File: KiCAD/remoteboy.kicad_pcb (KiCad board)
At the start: 2 copper layers, 47.2 x 129.2 mm, 36 parts, among them Q1 MMBT2222A, SW1 SW_Push, SW10 SW_Push, SW2 SW_Push, SW3 SW_Push, SW4 SW_Push, SW5 SW_Push, SW6 SW_Push, SW7 SW_Push, SW8 SW_Push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

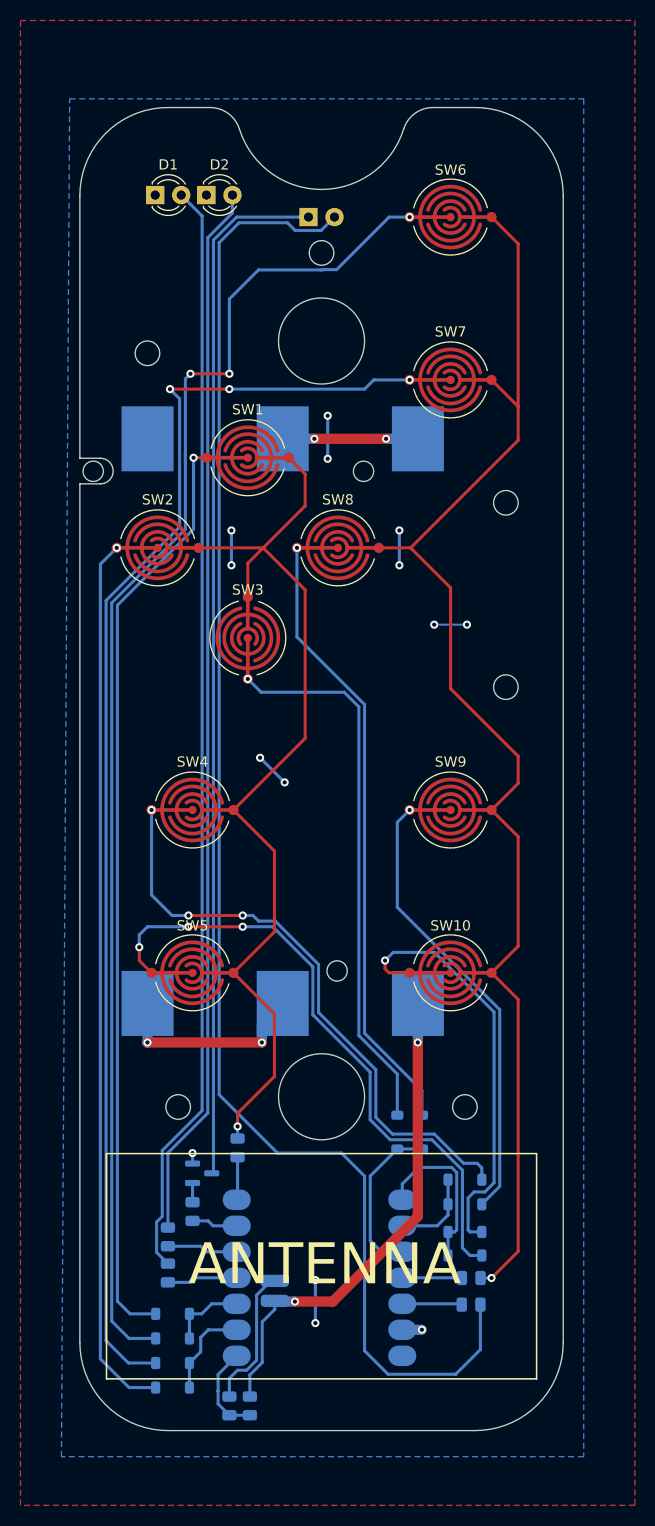
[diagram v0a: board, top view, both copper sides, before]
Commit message: Fix schematic and pcb
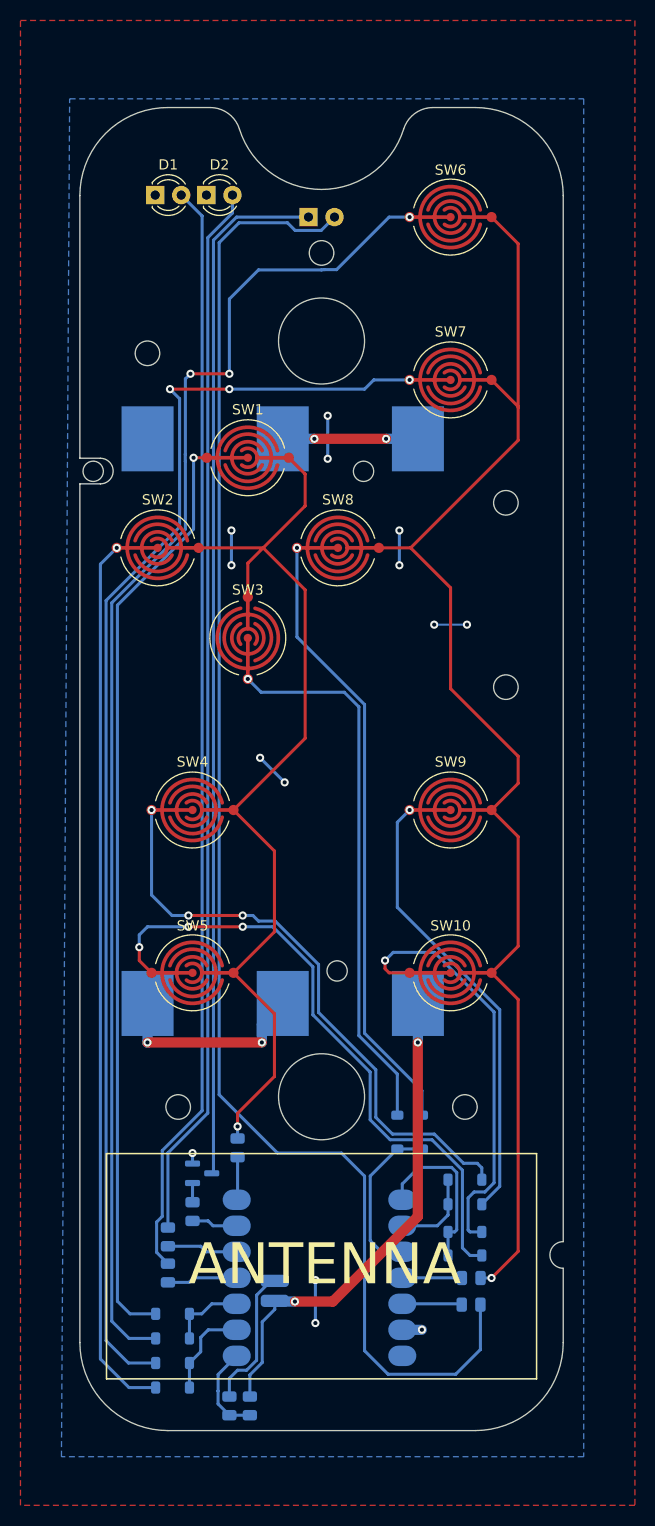
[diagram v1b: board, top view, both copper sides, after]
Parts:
- turned D10 to 0 degrees
- turned D11 to -90 degrees
- turned D12 to 180 degrees
- turned D13 to 180 degrees
- turned D4 to 0 degrees
- turned D5 to 0 degrees
- turned D6 to -90 degrees
- turned D7 to 180 degrees
- turned D8 to 180 degrees
- turned D9 to 0 degrees
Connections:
- D10 pad 1: /ROW2 -> Net-(D10-K)
- D10 pad 2: Net-(D10-A) -> /ROW2
- D11 pad 1: /ROW3 -> Net-(D11-K)
- D11 pad 2: Net-(D11-A) -> /ROW3
- D12 pad 1: /ROW4 -> Net-(D12-K)
- D12 pad 2: Net-(D12-A) -> /ROW4
- D13 pad 1: /ROW5 -> Net-(D13-K)
- D13 pad 2: Net-(D13-A) -> /ROW5
- D4 pad 1: /ROW1 -> Net-(D4-K)
- D4 pad 2: Net-(D4-A) -> /ROW1
- D5 pad 1: /ROW2 -> Net-(D5-K)
- D5 pad 2: Net-(D5-A) -> /ROW2
- D6 pad 1: /ROW3 -> Net-(D6-K)
- D6 pad 2: Net-(D6-A) -> /ROW3
- D7 pad 1: /ROW4 -> Net-(D7-K)
- D7 pad 2: Net-(D7-A) -> /ROW4
- D8 pad 1: /ROW5 -> Net-(D8-K)
- D8 pad 2: Net-(D8-A) -> /ROW5
- D9 pad 1: /ROW1 -> Net-(D9-K)
- D9 pad 2: Net-(D9-A) -> /ROW1
- SW1 pad 1: Net-(D4-A) -> Net-(D4-K)
- SW10 pad 1: Net-(D13-A) -> Net-(D13-K)
- SW2 pad 1: Net-(D5-A) -> Net-(D5-K)
- SW3 pad 1: Net-(D6-A) -> Net-(D6-K)
- SW4 pad 1: Net-(D7-A) -> Net-(D7-K)
- SW5 pad 1: Net-(D8-A) -> Net-(D8-K)
- SW6 pad 1: Net-(D9-A) -> Net-(D9-K)
- SW7 pad 1: Net-(D10-A) -> Net-(D10-K)
- SW8 pad 1: Net-(D11-A) -> Net-(D11-K)
- SW9 pad 1: Net-(D12-A) -> Net-(D12-K)
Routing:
- net Net-(D9-K): track 0.00 -> 132.7 mm, vias 0 -> 3
- net Net-(D9-A): track 132.7 -> 0.00 mm, vias 3 -> 0
- net Net-(D10-K): track 0.00 -> 126.0 mm, vias 0 -> 3
- net Net-(D10-A): track 126.0 -> 0.00 mm, vias 3 -> 0
- net Net-(D4-K): track 0.00 -> 91.0 mm, vias 0 -> 1
- net Net-(D4-A): track 91.0 -> 0.00 mm, vias 1 -> 0
- net Net-(D5-K): track 0.00 -> 86.4 mm, vias 0 -> 1
- net Net-(D5-A): track 86.4 -> 0.00 mm, vias 1 -> 0
- net Net-(D8-K): track 0.00 -> 61.2 mm, vias 0 -> 3
- net Net-(D8-A): track 61.2 -> 0.00 mm, vias 3 -> 0
- net Net-(D11-K): track 0.00 -> 60.5 mm, vias 0 -> 1
- net Net-(D11-A): track 60.5 -> 0.00 mm, vias 1 -> 0
- net Net-(D7-K): track 0.00 -> 58.2 mm, vias 0 -> 3
- net Net-(D7-A): track 58.2 -> 0.00 mm, vias 3 -> 0
- net Net-(D6-K): track 0.00 -> 53.4 mm, vias 0 -> 1
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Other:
- outline, holes or cut-outs redrawn
